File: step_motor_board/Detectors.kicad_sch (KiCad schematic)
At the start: 52 parts, among them J3 DI2 (DG141R-04), J4 DI1 (DG141R-04), J5 DI3 (DG141R-04), J6 DI4 (DG141R-04), U7 HEF40106BT (SO-14)

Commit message: DC, contr, mb, step v2
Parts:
- added R26 (x8): 1206-2 кОм±5%-0,25 Вт, Resistor_SMD:R_1206_3216Metric, symbol Device:R
- C25: renamed from C33; value 0,1uF 50V 0603 -> 0,1uF 100V 0603
- C25: value 0,1uF 50V 0603 -> 0,1uF 100V 0603
- C26: renamed from C27; value 0,1uF 50V 0603 -> 0,1uF 100V 0603
- C26: renamed from C34; value 0,1uF 50V 0603 -> 0,1uF 100V 0603
- C27: renamed from C35; value 0,1uF 50V 0603 -> 0,1uF 100V 0603
- C27: renamed from C29; value 0,1uF 50V 0603 -> 0,1uF 100V 0603
- C28: renamed from C31; value 0,1uF 50V 0603 -> 0,1uF 100V 0603
- C28: renamed from C36; value 0,1uF 50V 0603 -> 0,1uF 100V 0603
- C9: renamed from C22; value 0,1uF 100V 0805 -> 0,1uF 100V 0603; footprint PCM_Capacitor_SMD_AKL:C_0805_2012Metric_Pad1.18x1.45mm_HandSolder -> Capacitor_SMD:C_0603_1608Metric_Pad1.08x0.95mm_HandSolder
- J3: renamed from J5; value DI3 (DG141R-04) -> DG141R-2.54-04P-14-00A(H) (DI3)
- J3: value DI2 (DG141R-04) -> DG141R-2.54-04P-14-00A(H) (DI2)
- J4: value DI1 (DG141R-04) -> DG141R-2.54-04P-14-00A(H) (DI1)
- J4: renamed from J6; value DI4 (DG141R-04) -> DG141R-2.54-04P-14-00A(H) (DI4)
- R16: renamed from R25; value 0805-1 кОм±5%-0,125 Вт -> 0603-1 кОм±5%-0,0625 Вт; footprint PCM_Resistor_SMD_AKL:R_0805_2012Metric_Pad1.20x1.40mm_HandSolder -> Resistor_SMD:R_0603_1608Metric
- R18: renamed from R28; value 0805-1 кОм±5%-0,125 Вт -> 0603-1 кОм±5%-0,0625 Вт; footprint PCM_Resistor_SMD_AKL:R_0805_2012Metric_Pad1.20x1.40mm_HandSolder -> Resistor_SMD:R_0603_1608Metric
- R20: renamed from R31; value 0805-1 кОм±5%-0,125 Вт -> 0603-1 кОм±5%-0,0625 Вт; footprint PCM_Resistor_SMD_AKL:R_0805_2012Metric_Pad1.20x1.40mm_HandSolder -> Resistor_SMD:R_0603_1608Metric
- R22: renamed from R34; value 0805-1 кОм±5%-0,125 Вт -> 0603-1 кОм±5%-0,0625 Вт; footprint PCM_Resistor_SMD_AKL:R_0805_2012Metric_Pad1.20x1.40mm_HandSolder -> Resistor_SMD:R_0603_1608Metric
- R23: renamed from R36; value 0805-10 кОм±5%-0,125 Вт -> 0603-10 кОм±5%-0,0625 Вт; footprint PCM_Resistor_SMD_AKL:R_0805_2012Metric_Pad1.20x1.40mm_HandSolder -> Resistor_SMD:R_0603_1608Metric
- R24: renamed from R35; value 0805-10 кОм±5%-0,125 Вт -> 0603-10 кОм±5%-0,0625 Вт; footprint PCM_Resistor_SMD_AKL:R_0805_2012Metric_Pad1.20x1.40mm_HandSolder -> Resistor_SMD:R_0603_1608Metric
- R25: renamed from R37; value 0805-10 кОм±5%-0,125 Вт -> 0603-10 кОм±5%-0,0625 Вт; footprint PCM_Resistor_SMD_AKL:R_0805_2012Metric_Pad1.20x1.40mm_HandSolder -> Resistor_SMD:R_0603_1608Metric
- R26: renamed from R23; value 1206-1 кОм±5%-0,25 Вт -> 1206-2 кОм±5%-0,25 Вт; footprint PCM_Resistor_SMD_AKL:R_1206_3216Metric_Pad1.42x1.75mm_HandSolder -> Resistor_SMD:R_1206_3216Metric
- R26: value 1206-1 кОм±5%-0,25 Вт -> 1206-2 кОм±5%-0,25 Вт; footprint PCM_Resistor_SMD_AKL:R_1206_3216Metric_Pad1.42x1.75mm_HandSolder -> Resistor_SMD:R_1206_3216Metric
- R26: renamed from R38; value 0805-10 кОм±5%-0,125 Вт -> 0603-10 кОм±5%-0,0625 Вт; footprint PCM_Resistor_SMD_AKL:R_0805_2012Metric_Pad1.20x1.40mm_HandSolder -> Resistor_SMD:R_0603_1608Metric
- R26: renamed from R24; value 1206-1 кОм±5%-0,25 Вт -> 1206-2 кОм±5%-0,25 Вт; footprint PCM_Resistor_SMD_AKL:R_1206_3216Metric_Pad1.42x1.75mm_HandSolder -> Resistor_SMD:R_1206_3216Metric
- R26: renamed from R27; value 1206-1 кОм±5%-0,25 Вт -> 1206-2 кОм±5%-0,25 Вт; footprint PCM_Resistor_SMD_AKL:R_1206_3216Metric_Pad1.42x1.75mm_HandSolder -> Resistor_SMD:R_1206_3216Metric
- R26: renamed from R29; value 1206-1 кОм±5%-0,25 Вт -> 1206-2 кОм±5%-0,25 Вт; footprint PCM_Resistor_SMD_AKL:R_1206_3216Metric_Pad1.42x1.75mm_HandSolder -> Resistor_SMD:R_1206_3216Metric
- R26: renamed from R32; value 1206-1 кОм±5%-0,25 Вт -> 1206-2 кОм±5%-0,25 Вт; footprint PCM_Resistor_SMD_AKL:R_1206_3216Metric_Pad1.42x1.75mm_HandSolder -> Resistor_SMD:R_1206_3216Metric
- R26: renamed from R30; value 1206-1 кОм±5%-0,25 Вт -> 1206-2 кОм±5%-0,25 Вт; footprint PCM_Resistor_SMD_AKL:R_1206_3216Metric_Pad1.42x1.75mm_HandSolder -> Resistor_SMD:R_1206_3216Metric
- R26: renamed from R33; value 1206-1 кОм±5%-0,25 Вт -> 1206-2 кОм±5%-0,25 Вт; footprint PCM_Resistor_SMD_AKL:R_1206_3216Metric_Pad1.42x1.75mm_HandSolder -> Resistor_SMD:R_1206_3216Metric
- renumbered C26 to C29, C28 to C30, C30 to C31, OC1 to OC2, TP7 to TP1, TP16 to TP1, TP2 to TP11, TP6 to TP12, TP12 to TP13, TP15 to TP14, TP4 to TP15, TP13 to TP2, TP17 to TP2, TP1 to TP4, TP11 to TP6, TP14 to TP7
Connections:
- net +24V: now also R26.1, R26.1, R26.1, R26.1
- net at D3.1 (A1), R26.1, R26.2: now also R26.1, R26.2
- net at D4.1 (A1), R26.1, R26.2: now also R26.1, R26.2
- net at OC2.1, R26.2: now also R26.2
- net at OC2.3, R26.2: now also R26.2
- net at OC2.5, R26.2: now also R26.2
- net at OC2.7, R26.2: now also R26.2
- net at D5.1 (A1), R26.1, R26.2: now also R26.1, R26.2
- net at D6.1 (A1), R26.1, R26.2: now also R26.1, R26.2
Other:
- moved on the sheet: D3, D4, D5, D6, R23, R24, R25, R26, U7D, U7F

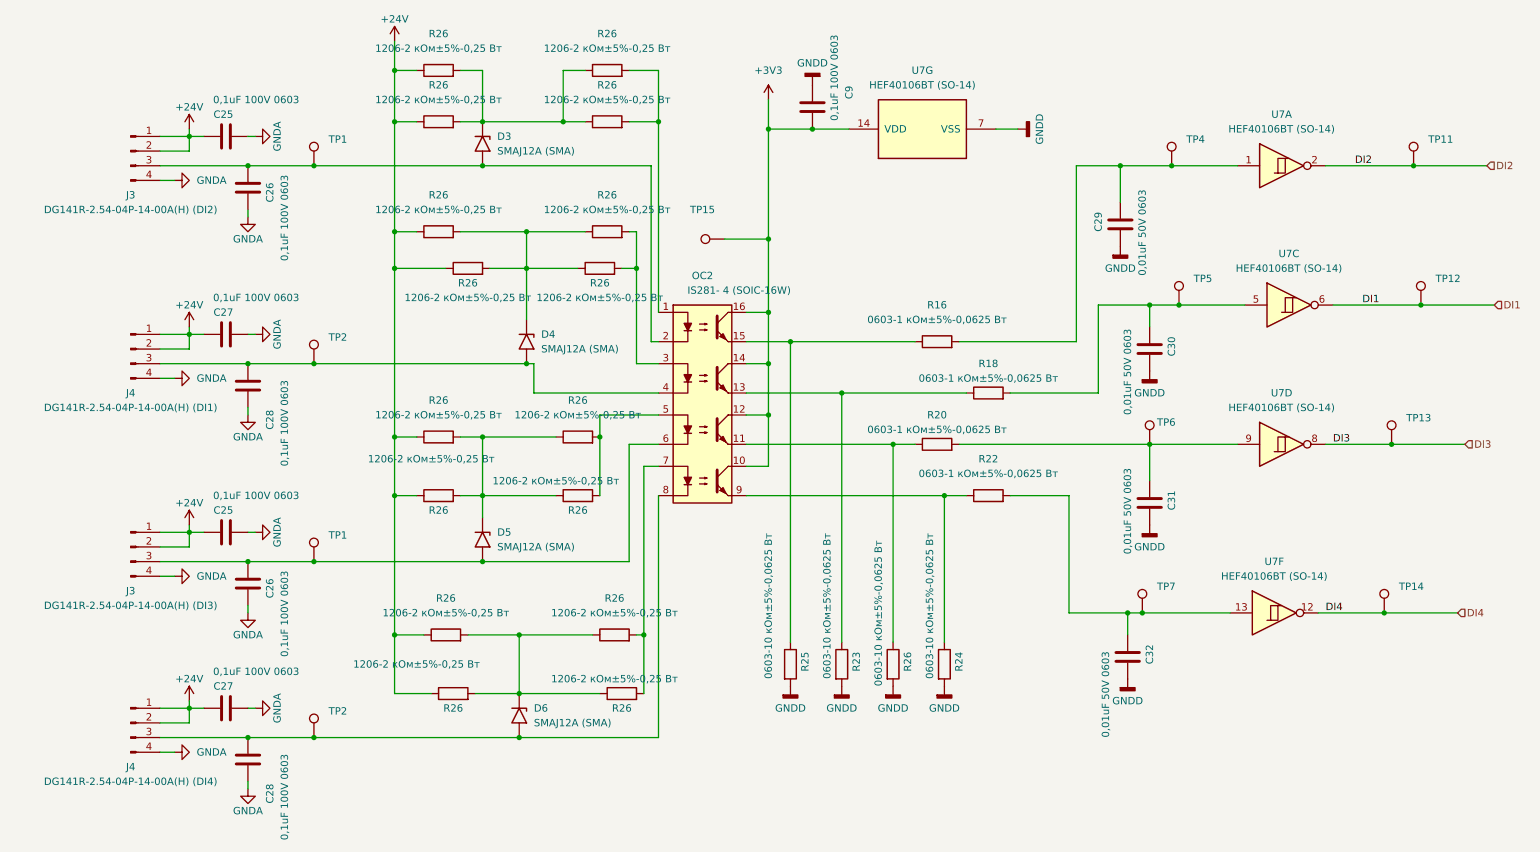
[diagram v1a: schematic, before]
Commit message: all замменил резисторы failsafe в плате контроллера и обрал из перечня во всех остальных
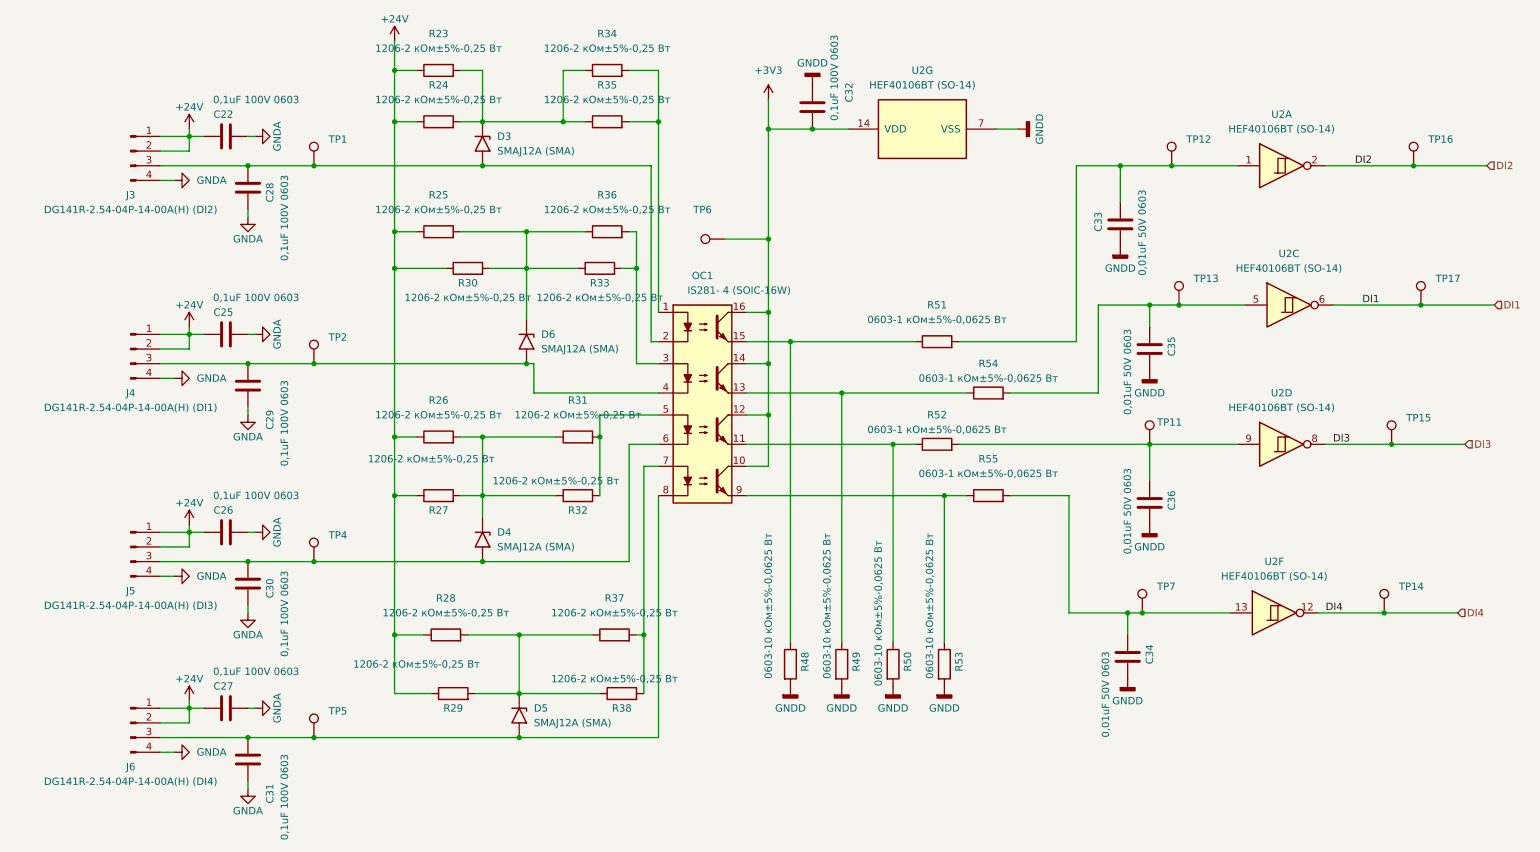
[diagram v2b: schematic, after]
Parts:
- C22, C26: renamed from C25; footprint Capacitor_SMD:C_0603_1608Metric_Pad1.08x0.95mm_HandSolder -> Capacitor_SMD:C_0603_1608Metric
- C25: renamed from C27; footprint Capacitor_SMD:C_0603_1608Metric_Pad1.08x0.95mm_HandSolder -> Capacitor_SMD:C_0603_1608Metric
- C27: footprint Capacitor_SMD:C_0603_1608Metric_Pad1.08x0.95mm_HandSolder -> Capacitor_SMD:C_0603_1608Metric
- C28, C30: renamed from C26; footprint Capacitor_SMD:C_0603_1608Metric_Pad1.08x0.95mm_HandSolder -> Capacitor_SMD:C_0603_1608Metric
- C29, C31: renamed from C28; footprint Capacitor_SMD:C_0603_1608Metric_Pad1.08x0.95mm_HandSolder -> Capacitor_SMD:C_0603_1608Metric
- C32: renamed from C9; footprint Capacitor_SMD:C_0603_1608Metric_Pad1.08x0.95mm_HandSolder -> Capacitor_SMD:C_0603_1608Metric
- C33: renamed from C29; footprint PCM_Capacitor_SMD_US_Handsoldering_AKL:C_0603_1608Metric_Pad1.08x0.95mm -> Capacitor_SMD:C_0603_1608Metric
- C34: renamed from C32; footprint PCM_Capacitor_SMD_US_Handsoldering_AKL:C_0603_1608Metric_Pad1.08x0.95mm -> Capacitor_SMD:C_0603_1608Metric
- C35: renamed from C30; footprint PCM_Capacitor_SMD_US_Handsoldering_AKL:C_0603_1608Metric_Pad1.08x0.95mm -> Capacitor_SMD:C_0603_1608Metric
- C36: renamed from C31; footprint PCM_Capacitor_SMD_US_Handsoldering_AKL:C_0603_1608Metric_Pad1.08x0.95mm -> Capacitor_SMD:C_0603_1608Metric
- OC1: renamed from OC2; footprint PCM_Package_SO_AKL:SOIC-16W_5.3x10.2mm_P1.27mm -> Package_SO:SOIC-16W_5.3x10.2mm_P1.27mm
- TP1, TP14, TP2, TP7: footprint PCM_4ms_TestPoint:TestPoint_D1 -> TestPoint:TestPoint_Pad_D1.0mm
- TP11: renamed from TP6; footprint PCM_4ms_TestPoint:TestPoint_D1 -> TestPoint:TestPoint_Pad_D1.0mm
- TP12: renamed from TP4; footprint PCM_4ms_TestPoint:TestPoint_D1 -> TestPoint:TestPoint_Pad_D1.0mm
- TP13: renamed from TP5; footprint PCM_4ms_TestPoint:TestPoint_D1 -> TestPoint:TestPoint_Pad_D1.0mm
- TP15: renamed from TP13; footprint PCM_4ms_TestPoint:TestPoint_D1 -> TestPoint:TestPoint_Pad_D1.0mm
- TP16: renamed from TP11; footprint PCM_4ms_TestPoint:TestPoint_D1 -> TestPoint:TestPoint_Pad_D1.0mm
- TP17: renamed from TP12; footprint PCM_4ms_TestPoint:TestPoint_D1 -> TestPoint:TestPoint_Pad_D1.0mm
- TP4: renamed from TP1; footprint PCM_4ms_TestPoint:TestPoint_D1 -> TestPoint:TestPoint_Pad_D1.0mm
- TP5: renamed from TP2; footprint PCM_4ms_TestPoint:TestPoint_D1 -> TestPoint:TestPoint_Pad_D1.0mm
- TP6: renamed from TP15; footprint PCM_4ms_TestPoint:TestPoint_D1 -> TestPoint:TestPoint_Pad_D1.0mm
- renumbered D5 to D4, D6 to D5, D4 to D6, J3 to J5, J4 to J6, R26 to R23, R26 to R24, R26 to R25, R26 to R27, R26 to R28, R26 to R29, R26 to R30, R26 to R31, R26 to R32, R26 to R33, R26 to R34, R26 to R35, R26 to R36, R26 to R37, R26 to R38, R25 to R48, R23 to R49, R26 to R50, R16 to R51, R20 to R52, R24 to R53, R18 to R54, R22 to R55, U7 to U2

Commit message: update schemas
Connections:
- net DI1: now also TP16.1, U2.2; no longer TP17.1, U2.6
- net DI2: now also TP17.1, U2.6; no longer TP16.1, U2.2
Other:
- moved on the sheet: TP6
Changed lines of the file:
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@@
 (kicad_sch
-	(version 20231120)
+	(version 20250114)
 	(generator "eeschema")
-	(generator_version "8.0")
+	(generator_version "9.0")
 	(paper "A4")
 	(junction
@@
 	(wire
 		(pts
-			(xy 101.6 81.28) (xy 100.33 81.28)
-		)
-		(stroke
-			(width 0)
-			(type default)
-		)
-	)
-	(wire
-		(pts
 			(xy 90.17 128.27) (xy 99.06 128.27)
 		)
@@
 	(wire
 		(pts
-			(xy 101.6 86.36) (xy 123.19 86.36)
+			(xy 100.33 86.36) (xy 123.19 86.36)
 		)
 		(stroke
@@
 	(wire
 		(pts
-			(xy 101.6 86.36) (xy 101.6 81.28)
+			(xy 100.33 86.36) (xy 100.33 81.28)
 		)
 		(stroke
@@
 	(wire
 		(pts
-			(xy 134.62 59.69) (xy 142.24 59.69)
+			(xy 140.97 59.69) (xy 142.24 59.69)
 		)
 		(stroke
@@
 	(label "DI3"
 		(at 240.03 95.25 0)
-		(fields_autoplaced yes)
 		(effects
 			(font
@@
 		)
 	)
-	(label "DI2"
+	(label "DI1"
 		(at 243.84 46.99 0)
-		(fields_autoplaced yes)
 		(effects
 			(font
@@
 		)
 	)
-	(label "DI1"
+	(label "DI2"
 		(at 245.11 71.12 0)
-		(fields_autoplaced yes)
 		(effects
 			(font
@@
 	(label "DI4"
 		(at 238.76 124.46 0)
-		(fields_autoplaced yes)
 		(effects
 			(font
@@
 		)
 	)
-	(hierarchical_label "DI2"
+	(hierarchical_label "DI1"
 		(shape input)
 		(at 266.7 46.99 0)
-		(fields_autoplaced yes)
 		(effects
 			(font
@@
 		(shape input)
 		(at 262.89 95.25 0)
-		(fields_autoplaced yes)
 		(effects
 			(font
@@
 		)
 	)
-	(hierarchical_label "DI1"
+	(hierarchical_label "DI2"
 		(shape input)
 		(at 267.97 71.12 0)
-		(fields_autoplaced yes)
 		(effects
 			(font
@@
 		(shape input)
 		(at 261.62 124.46 0)
-		(fields_autoplaced yes)
 		(effects
 			(font
@@
 	(symbol
 		(lib_id "Connector:TestPoint")
-		(at 134.62 59.69 90)
+		(at 140.97 59.69 90)
 		(unit 1)
 		(exclude_from_sim no)
@@
 		(dnp no)
 		(property "Reference" "TP6"
-			(at 130.81 54.61 90)
+			(at 137.16 54.61 90)
 			(effects
 				(font
@@
 		)
 		(property "Value" "TestPoint"
-			(at 131.318 57.15 90)
+			(at 137.668 57.15 90)
 			(effects
 				(font
@@
 		)
 		(property "Footprint" "TestPoint:TestPoint_Pad_D1.0mm"
-			(at 134.62 54.61 0)
+			(at 140.97 54.61 0)
 			(effects
 				(font
@@
 		)
 		(property "Datasheet" "~"
-			(at 134.62 54.61 0)
+			(at 140.97 54.61 0)
 			(effects
 				(font
@@
 		)
 		(property "Description" ""
-			(at 134.62 59.69 0)
+			(at 140.97 59.69 0)
 			(effects
 				(font
